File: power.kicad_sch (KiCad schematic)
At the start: 17 parts, among them U1 TL072, U2 TL074, U3 TL074, U4 TL074

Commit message: Finish placing
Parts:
- U2, U3: footprint Package_SO:SOIC-14-16_3.9x9.9mm_P1.27mm -> Package_SO:SOIC-14_3.9x8.7mm_P1.27mm
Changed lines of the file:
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@@
       (effects (font (size 1.27 1.27)) (justify left))
     )
-    (property "Footprint" "Package_SO:SOIC-14-16_3.9x9.9mm_P1.27mm" (at 163.83 62.23 0)
+    (property "Footprint" "Package_SO:SOIC-14_3.9x8.7mm_P1.27mm" (at 163.83 62.23 0)
       (effects (font (size 1.27 1.27)) hide)
     )
@@
       (effects (font (size 1.27 1.27)) (justify left))
     )
-    (property "Footprint" "Package_SO:SOIC-14-16_3.9x9.9mm_P1.27mm" (at 140.97 59.69 0)
+    (property "Footprint" "Package_SO:SOIC-14_3.9x8.7mm_P1.27mm" (at 140.97 59.69 0)
       (effects (font (size 1.27 1.27)) hide)
     )

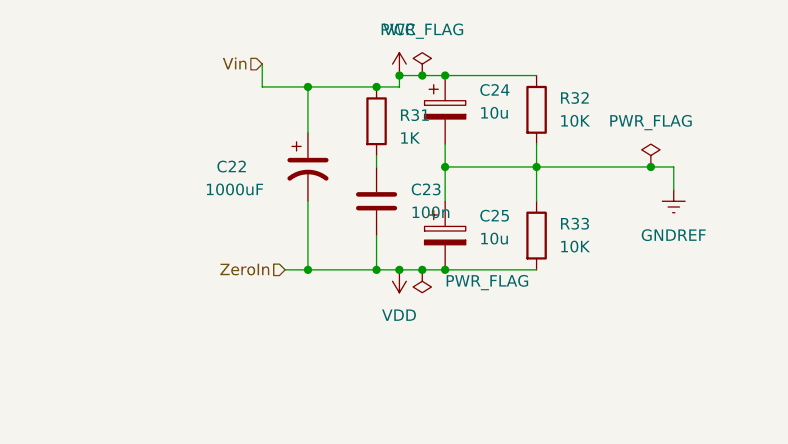
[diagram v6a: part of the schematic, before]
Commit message: fix gain stage for DC offset and some changes to power filtration
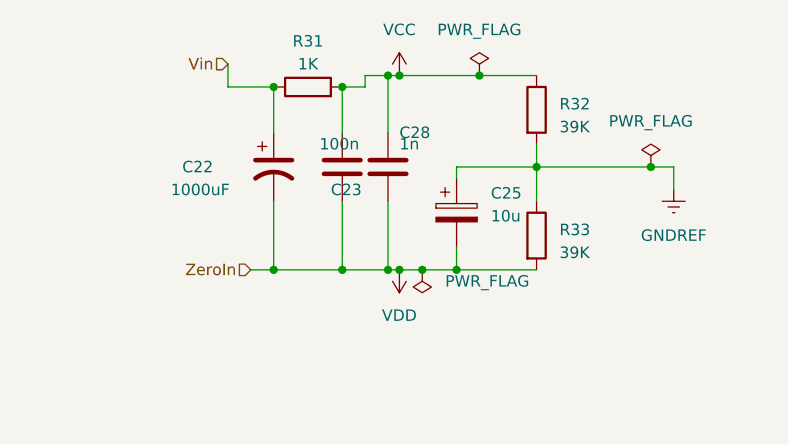
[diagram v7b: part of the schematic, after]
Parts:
- removed C24: 10u, Capacitor_THT:CP_Radial_D8.0mm_P3.50mm, symbol Device:C_Polarized
- added C28: 1n, Capacitor_SMD:C_0805_2012Metric_Pad1.18x1.45mm_HandSolder, symbol Device:C
- C25: footprint Capacitor_THT:CP_Radial_D8.0mm_P3.50mm -> Capacitor_THT:CP_Radial_D5.0mm_P2.50mm
- R32, R33: value 10K -> 39K
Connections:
- net VCC: now also C23.1, R31.2, C28.1; no longer C22.1, R30.1, R31.1
- net VDD: now also C28.2
- new net Vin: C22.1, R30.1, R31.1
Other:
- moved on the sheet: C22, C23, C25, R31
